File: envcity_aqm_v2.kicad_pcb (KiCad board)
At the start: 2 copper layers, 100 x 100 mm, 134 parts, among them IC1 DS1307ZN+, IC2 DMMT5401-7F, IC3 DMMT5401-7F, IC4 DMMT5401-7-F, IC6 ESP32-S2-SOLO-N4R2, J1 USB_B_Micro, J12 Conn_01x06_Male, J13 Conn_01x06_Male, J14 Conn_01x08_Pin, J15 Conn_01x02_Male, J16 Conn_01x02_Male, J2 Screw_Terminal_01x02, J3 Screw_Terminal_01x02, J6 Conn_01x04_Male, J7 Conn_01x06_Pin, J8 503398-1892, Q1 DMG2301L / DMP2045U, Q2 DMG2301L / DMP2045U, Q3 DMG2301L, Q4 DMG2301L, Q5 DMG2301L / DMP2045U, Q6 DMG2301L, Q7 DMN10H220L, Q8 DMN10H220L, SW1 RESET, SW2 BOOT, U1 TP4056, U10 RFM95W-915S2, U11 ADS1115IDGS, U12 TPS54202DDC, U2 USBLC6-2SC6, U3 MT3608, U4 SHT30-DIS, U6 AP2112K-3.3, U7 DHT11, U8 AP2112K-3.3, U9 74HC4067DB, Y2 AB26TRB

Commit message: altera componentes
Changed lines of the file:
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@@
     (fp_line (start 1 0.6) (end 1 -0.6)
       (stroke (width 0.1) (type solid)) (layer "F.Fab"))
-    (pad "1" smd roundrect (at -1.025 0 180) (size 1.15 1.4) (layers "F.Cu" "F.Paste" "F.Mask") (roundrect_rratio 0.217391)
+    (pad "1" smd roundrect (at -1.025 0 180) (size 1.15 1.4) (layers "F.Cu" "F.Paste" "F.Mask") (roundrect_rratio 0.2173913043)
       (net 14 "Net-(D3-K)") (pinfunction "K") (pintype "passive"))
-    (pad "2" smd roundrect (at 1.025 0 180) (size 1.15 1.4) (layers "F.Cu" "F.Paste" "F.Mask") (roundrect_rratio 0.217391)
+    (pad "2" smd roundrect (at 1.025 0 180) (size 1.15 1.4) (layers "F.Cu" "F.Paste" "F.Mask") (roundrect_rratio 0.2173913043)
       (net 3 "+5V") (pinfunction "A") (pintype "passive"))
     (model "${KICAD6_3DMODEL_DIR}/LED_SMD.3dshapes/LED_0805_2012Metric.wrl"
@@
     (fp_line (start 1 0.6) (end 1 -0.6)
       (stroke (width 0.1) (type solid)) (layer "F.Fab"))
-    (pad "1" smd roundrect (at -1.025 0 180) (size 1.15 1.4) (layers "F.Cu" "F.Paste" "F.Mask") (roundrect_rratio 0.217391)
+    (pad "1" smd roundrect (at -1.025 0 180) (size 1.15 1.4) (layers "F.Cu" "F.Paste" "F.Mask") (roundrect_rratio 0.2173913043)
       (net 15 "Net-(D4-K)") (pinfunction "K") (pintype "passive"))
-    (pad "2" smd roundrect (at 1.025 0 180) (size 1.15 1.4) (layers "F.Cu" "F.Paste" "F.Mask") (roundrect_rratio 0.217391)
+    (pad "2" smd roundrect (at 1.025 0 180) (size 1.15 1.4) (layers "F.Cu" "F.Paste" "F.Mask") (roundrect_rratio 0.2173913043)
       (net 3 "+5V") (pinfunction "A") (pintype "passive"))
     (model "${KICAD6_3DMODEL_DIR}/LED_SMD.3dshapes/LED_0805_2012Metric.wrl"
@@
     (fp_line (start 1 0.6) (end 1 -0.6)
       (stroke (width 0.1) (type solid)) (layer "F.Fab"))
-    (pad "1" smd roundrect (at -1.025 0) (size 1.15 1.4) (layers "F.Cu" "F.Paste" "F.Mask") (roundrect_rratio 0.217391)
+    (pad "1" smd roundrect (at -1.025 0) (size 1.15 1.4) (layers "F.Cu" "F.Paste" "F.Mask") (roundrect_rratio 0.2173913043)
       (net 2 "GND") (pinfunction "K") (pintype "passive"))
-    (pad "2" smd roundrect (at 1.025 0) (size 1.15 1.4) (layers "F.Cu" "F.Paste" "F.Mask") (roundrect_rratio 0.217391)
+    (pad "2" smd roundrect (at 1.025 0) (size 1.15 1.4) (layers "F.Cu" "F.Paste" "F.Mask") (roundrect_rratio 0.2173913043)
       (net 20 "Net-(D13-A)") (pinfunction "A") (pintype "passive"))
     (model "${KICAD6_3DMODEL_DIR}/LED_SMD.3dshapes/LED_0805_2012Metric.wrl"
@@
     (fp_line (start 1 0.6) (end 1 -0.6)
       (stroke (width 0.1) (type solid)) (layer "F.Fab"))
-    (pad "1" smd roundrect (at -1.025 0) (size 1.15 1.4) (layers "F.Cu" "F.Paste" "F.Mask") (roundrect_rratio 0.217391)
+    (pad "1" smd roundrect (at -1.025 0) (size 1.15 1.4) (layers "F.Cu" "F.Paste" "F.Mask") (roundrect_rratio 0.2173913043)
       (net 2 "GND") (pinfunction "K") (pintype "passive"))
-    (pad "2" smd roundrect (at 1.025 0) (size 1.15 1.4) (layers "F.Cu" "F.Paste" "F.Mask") (roundrect_rratio 0.217391)
+    (pad "2" smd roundrect (at 1.025 0) (size 1.15 1.4) (layers "F.Cu" "F.Paste" "F.Mask") (roundrect_rratio 0.2173913043)
       (net 19 "Net-(D14-A)") (pinfunction "A") (pintype "passive"))
     (model "${KICAD6_3DMODEL_DIR}/LED_SMD.3dshapes/LED_0805_2012Metric.wrl"
@@
     (fp_line (start 1.6 0.8) (end -1.6 0.8)
       (stroke (width 0.1) (type solid)) (layer "F.Fab"))
-    (pad "1" smd roundrect (at -1.475 0 180) (size 1.15 1.8) (layers "F.Cu" "F.Paste" "F.Mask") (roundrect_rratio 0.217391)
+    (pad "1" smd roundrect (at -1.475 0 180) (size 1.15 1.8) (layers "F.Cu" "F.Paste" "F.Mask") (roundrect_rratio 0.2173913043)
       (net 6 "Vsolar_reg") (pintype "passive") (zone_connect 2))
-    (pad "2" smd roundrect (at 1.475 0 180) (size 1.15 1.8) (layers "F.Cu" "F.Paste" "F.Mask") (roundrect_rratio 0.217391)
+    (pad "2" smd roundrect (at 1.475 0 180) (size 1.15 1.8) (layers "F.Cu" "F.Paste" "F.Mask") (roundrect_rratio 0.2173913043)
       (net 2 "GND") (pintype "passive"))
     (model "${KICAD6_3DMODEL_DIR}/Capacitor_SMD.3dshapes/C_1206_3216Metric.wrl"
@@
     (fp_line (start 1.6 0.8) (end -1.6 0.8)
       (stroke (width 0.1) (type solid)) (layer "F.Fab"))
-    (pad "1" smd roundrect (at -1.475 0 90) (size 1.15 1.8) (layers "F.Cu" "F.Paste" "F.Mask") (roundrect_rratio 0.217391)
+    (pad "1" smd roundrect (at -1.475 0 90) (size 1.15 1.8) (layers "F.Cu" "F.Paste" "F.Mask") (roundrect_rratio 0.2173913043)
       (net 5 "Vsolar_protected") (pintype "passive") (zone_connect 2))
-    (pad "2" smd roundrect (at 1.475 0 90) (size 1.15 1.8) (layers "F.Cu" "F.Paste" "F.Mask") (roundrect_rratio 0.217391)
+    (pad "2" smd roundrect (at 1.475 0 90) (size 1.15 1.8) (layers "F.Cu" "F.Paste" "F.Mask") (roundrect_rratio 0.2173913043)
       (net 2 "GND") (pintype "passive"))
     (model "${KICAD6_3DMODEL_DIR}/Capacitor_SMD.3dshapes/C_1206_3216Metric.wrl"
@@
   (segment (start 149.05 117.7875) (end 148.1 118.7375) (width 0.25) (layer "F.Cu") (net 6))
   (segment (start 135.96 129.5) (end 136.75 129.5) (width 0.25) (layer "F.Cu") (net 6))
-  (segment (start 124.6 112) (end 123.8 111.2) (width 0.25) (layer "F.Cu") (net 6))
+  (segment (start 124.55 111.2) (end 122.625 111.2) (width 0.25) (layer "F.Cu") (net 6))
   (segment (start 147.475 118.7375) (end 147.475 119.6875) (width 0.5) (layer "F.Cu") (net 6))
-  (segment (start 123.8 111.2) (end 122.625 111.2) (width 0.25) (layer "F.Cu") (net 6))
   (segment (start 148.1 118.7375) (end 147.475 118.7375) (width 0.25) (layer "F.Cu") (net 6))
   (segment (start 142.475 122.75) (end 142.475 123.975) (width 0.5) (layer "F.Cu") (net 6))
   (segment (start 139.3 114.3) (end 139.435 114.435) (width 0.25) (layer "F.Cu") (net 6))
+  (segment (start 126.95 113.6) (end 124.55 111.2) (width 0.25) (layer "F.Cu") (net 6))
   (segment (start 135.96 130.71) (end 136 130.75) (width 0.25) (layer "F.Cu") (net 6))
-  (via (at 124.6 112) (size 0.6) (drill 0.3) (layers "F.Cu" "B.Cu") (net 6))
+  (segment (start 134.85 113.6) (end 126.95 113.6) (width 0.25) (layer "F.Cu") (net 6))
+  (via (at 134.85 113.6) (size 0.6) (drill 0.3) (layers "F.Cu" "B.Cu") (net 6))
   (via (at 139.3 114.3) (size 0.6) (drill 0.3) (layers "F.Cu" "B.Cu") (net 6))
-  (segment (start 126.9 114.3) (end 124.6 112) (width 0.25) (layer "B.Cu") (net 6))
-  (segment (start 139.3 114.3) (end 126.9 114.3) (width 0.25) (layer "B.Cu") (net 6))
+  (segment (start 134.85 113.6) (end 135.55 114.3) (width 0.25) (layer "B.Cu") (net 6))
+  (segment (start 135.55 114.3) (end 139.3 114.3) (width 0.25) (layer "B.Cu") (net 6))
   (segment (start 137.6 96.6) (end 137.6 97.975) (width 0.5) (layer "F.Cu") (net 8))
   (segment (start 136.6 98.975) (end 136.6 102.5) (width 0.5) (layer "F.Cu") (net 8))
@@
         (xy 125.05 122.6)
         (xy 130 122.6)
-        (xy 130 122.6)
       )

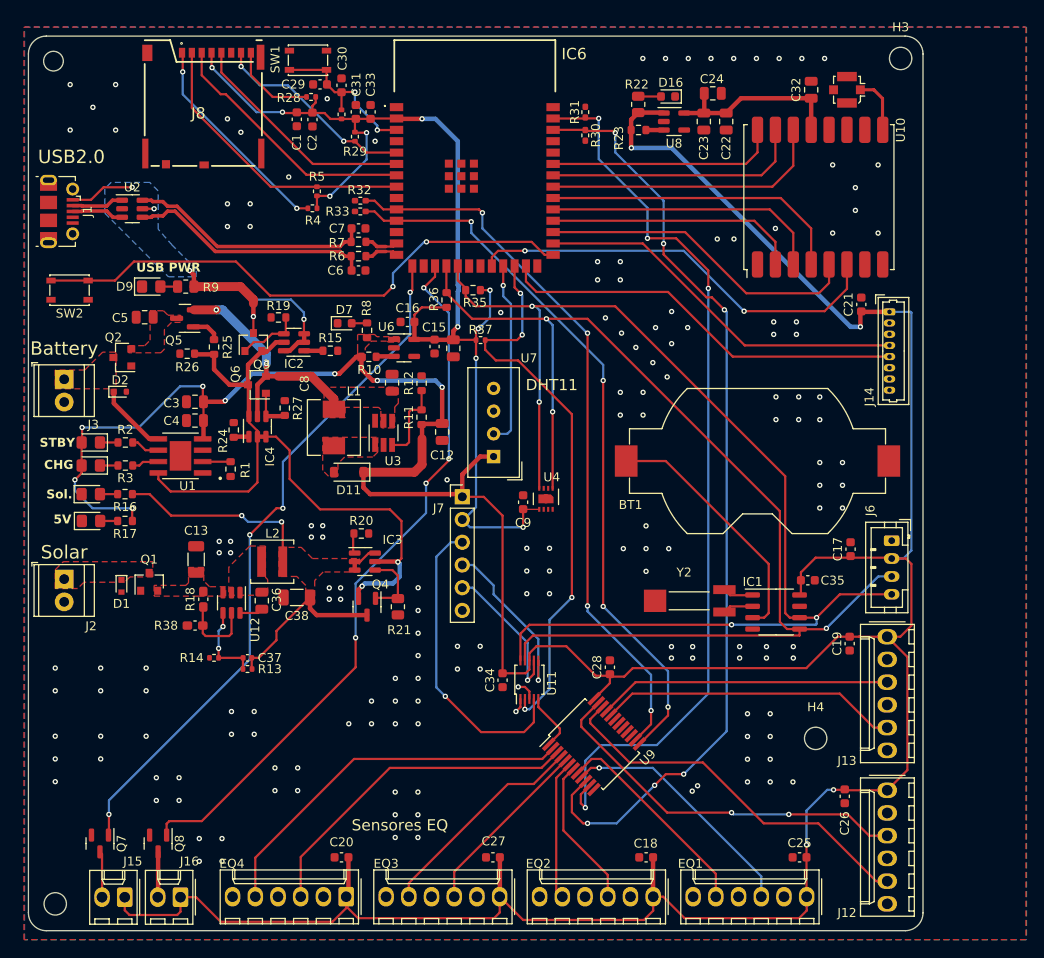
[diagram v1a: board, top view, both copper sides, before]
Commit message: Add logo na pcb
Add a logo
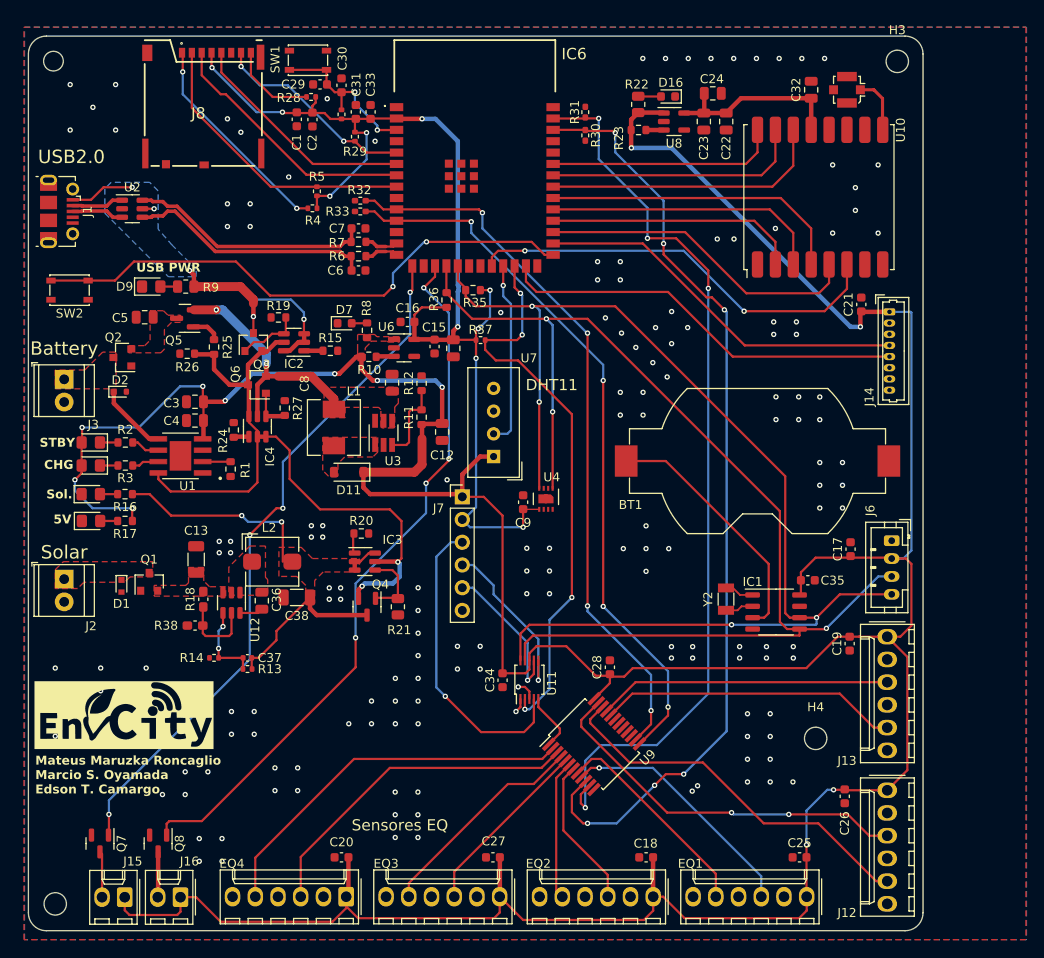
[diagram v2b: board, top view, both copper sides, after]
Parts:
- added G***: LOGO, AB26TRB-32.768KHZ-T:envcity_logo_kicad_sm, F.Cu at (121.7, 135.9)
- added G***: LOGO, AB26TRB-32.768KHZ-T:envcity_logo_kicad_sm, B.Cu at (200.2, 72.4)
- BT1: value Battery_Cell -> CR2032-BS-6-1
- D1: value D_TVS_ALT -> HESD5Z24
- D2: value D_TVS_ALT -> VESD05A1
- L2: value 6.8uH -> SRP5030T-100M; footprint Inductor_SMD:L_Coilcraft_XAL4030-XXX -> Inductor_SMD:L_Bourns_SRP5030T
- Q1, Q2, Q5: value DMG2301L / DMP2045U -> DMP2045U-7
- Q3, Q4, Q6: value DMG2301L -> DMP2045U-7
- U10: value RFM95W-915S2 -> RFM95W-915
- Y2: value AB26TRB -> FC-135R; footprint AB26TRB-32.768KHZ-T:XTAL_AB26TRB-32.768KHZ-T -> Crystal:Crystal_SMD_3215-2Pin_3.2x1.5mm
- moved Y2 4.06 mm to (189.0, 122.9), turned to 90 degrees
- moved H3 0.50 mm to (208.1, 62.8)
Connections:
- net Net-(IC1-X1) renamed /CRYSTAL+
- net Net-(IC1-X2) renamed /CRYSTAL-
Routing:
- net GND: vias 164 -> 161
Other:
- board text added: "Mateus Maruzka Roncaglio Marcio S. Oyamada Edson T. Camargo"

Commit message: add novo esp32
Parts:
- removed D16, D7: LED, LED_SMD:LED_0603_1608Metric
- removed IC6: ESP32-S2-SOLO-N4R2, ESP32-S2-SOLO-N4R2:ESP32S2SOLON4R2
- removed R22: 10k, Resistor_SMD:R_0805_2012Metric
- removed R8: 10k, Resistor_SMD:R_0603_1608Metric
- added IC5: ESP32-S3-WROOM-1-N16, ESP32-S3:ESP32S3WROOM1N16, F.Cu at (160.8, 73.2)
- D2: footprint Diode_SMD:D_SOD-523 -> AB26TRB-32.768KHZ-T:PESD24VS1ULQZ
- IC4: value DMMT5401-7-F -> DMMT5401-7F
- R18, R38: footprint Capacitor_SMD:C_0603_1608Metric_Pad1.08x0.95mm_HandSolder -> Resistor_SMD:R_0603_1608Metric
- R30, R31, R32, R33: footprint Resistor_SMD:R_0402_1005Metric_Pad0.72x0.64mm_HandSolder -> Resistor_SMD:R_0402_1005Metric
- moved L2 0.52 mm to (138.3, 118.2)
- moved D2 0.46 mm to (120.9, 99.4)
- moved Q7 0.23 mm to (119.2, 150.2)
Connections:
- Q7 pad 1: /FAN1 -> /FAN2
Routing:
- net /FAN1: track 77.9 -> 0.00 mm, vias 4 -> 0
- net /FAN2: track 80.4 -> 88.2 mm
- net Net-(D16-A): track 2.52 -> 0.00 mm
- net Net-(D7-A): track 1.62 -> 0.00 mm
- net GND: vias 161 -> 176
